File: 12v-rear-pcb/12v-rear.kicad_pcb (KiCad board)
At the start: 2 copper layers, 11 parts

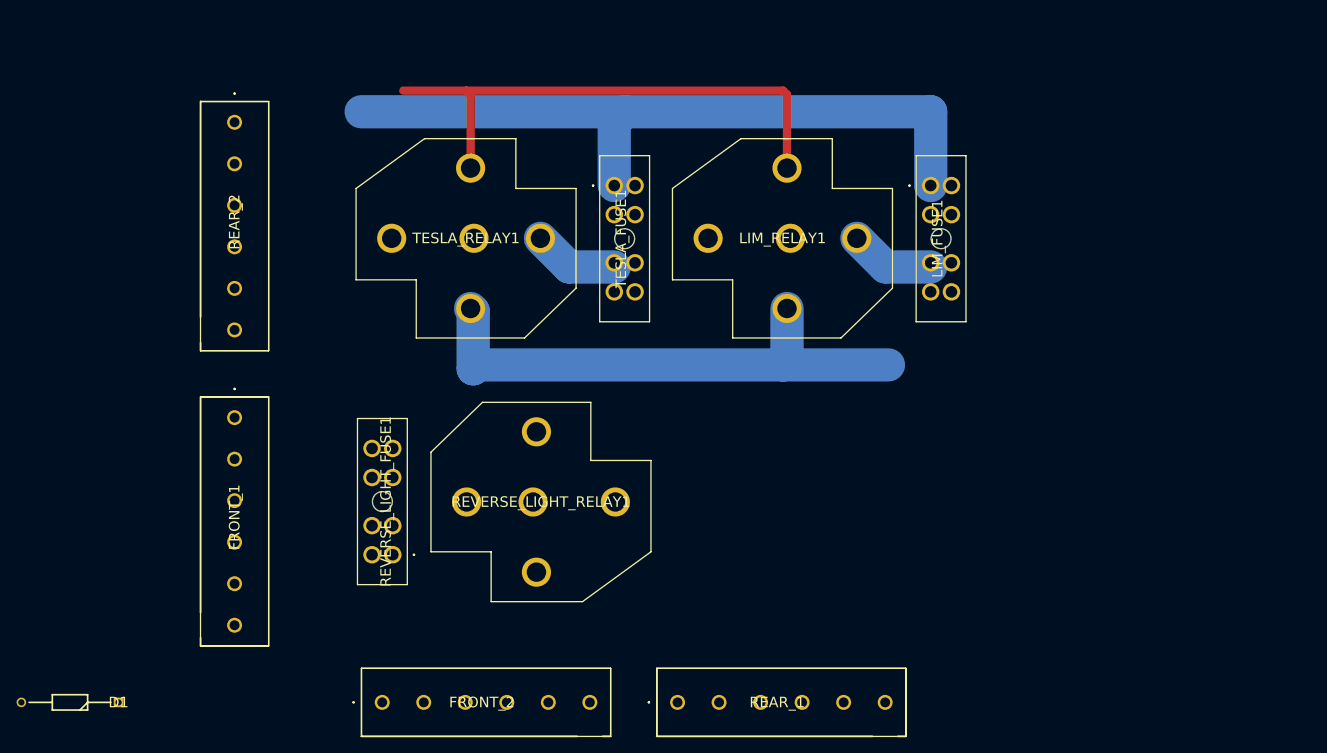
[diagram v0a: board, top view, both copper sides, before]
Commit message: Add dash vcu
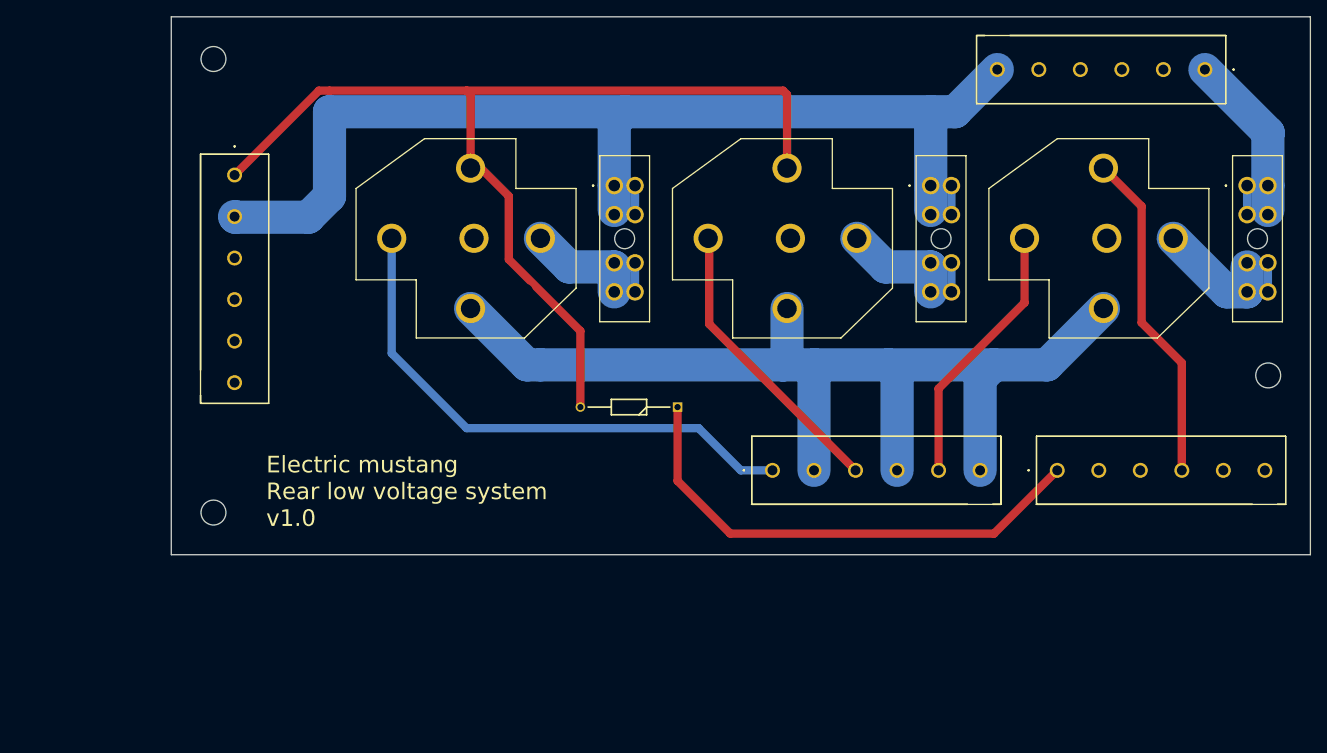
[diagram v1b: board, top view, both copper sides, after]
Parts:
- added H1: MountingHole, MountingHole:MountingHole_3mm, F.Cu at (54.6, 69.8)
- added H2: MountingHole, MountingHole:MountingHole_3mm, F.Cu at (54.6, 124.5)
- added H3: MountingHole, MountingHole:MountingHole_3mm, F.Cu at (181.6, 108.0)
- moved FRONT_1 124.1 mm to (174.0, 71.1), turned to 180 degrees
- moved REVERSE_LIGHT_FUSE1 112.1 mm to (179.1, 85.1), turned to 270 degrees
- moved REVERSE_LIGHT_RELAY1 90.8 mm to (170.2, 91.4), turned to 180 degrees
- moved FRONT_2 85.9 mm to (156.2, 119.4)
- moved D1 76.1 mm to (110.5, 111.8)
- moved REAR_1 30.2 mm to (121.9, 119.4)
- moved REAR_2 6.35 mm to (57.1, 83.8)
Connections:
- net LH_REAR_INDICATOR renamed Net-(FRONT_1-Pad2)
- net RH_REAR_INDICATOR renamed Net-(FRONT_1-Pad3)
- REAR_1 pad 4: LIM_GND -> GND
- REAR_1 pad 5: Net-(REAR_1-Pad5) -> REVERSE_LIGHT
- REAR_2 pad 1: REVERSE_LIGHT -> CHARGER_SWITCH_B
- REAR_2 pad 3: CHARGER_SWITCH_B -> Net-(REAR_2-Pad3)
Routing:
- net TESLA_12V: track 0.00 -> 65.5 mm
- net GND: track 64.6 -> 128.1 mm
- net CHARGER_ON_SIGNAL: track 0.00 -> 60.4 mm
- net CHARGER_SWITCH_A: track 86.9 -> 146.5 mm
- net CHARGER_SWITCH_B: track 64.8 -> 124.3 mm
- net REVERSE_SIGNAL: track 0.00 -> 40.3 mm
- net LIM_12V: track 0.00 -> 35.3 mm
- net REVERSE_LIGHT: track 0.00 -> 32.2 mm
- net IGNITION_12V: track 0.00 -> 28.6 mm
- net Net-(REVERSE_LIGHT_FUSE1-Pad3): track 0.00 -> 23.1 mm
- net Net-(TESLA_FUSE1-Pad3): track 10.3 -> 21.8 mm
- net Net-(LIM_FUSE1-Pad3): track 10.3 -> 21.8 mm
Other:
- board outline added: 137.2 x 64.8 mm
- board text added: "Electric mustang Rear low voltage system v1.0"

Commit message: 12v rear
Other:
- net class Default removed
